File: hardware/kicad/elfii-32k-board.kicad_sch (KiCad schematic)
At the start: 14 parts, among them J1 ELFII_P3_86, SW1 RAM_PAGE_ENABLE, U1 74HC573, U2 CY62256-70PC, U3 74LS151, U4 CD4011

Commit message: Rewire Hyperboard-derived schematic from actual pin geometry
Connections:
- net ~MWR is gone; now on net MA0: J1.64 (MA0)
- net +5V: now also J1.1 (+5V), J1.2 (+5V), U1.20 (VCC), U2.28 (VCC), U3.16 (VCC), U4.14 (VDD); no longer J1.85 (DISP_STAT), J1.86 (BUS_CLK), SW1.1 (L0), SW1.2 (L1), SW1.3 (L2), SW1.4 (L3), SW1.5 (L4), SW1.6 (L5), SW1.7 (L6), SW1.8 (L7), U2.3 (A7)
- net A10: now also U1.14 (Q5), U2.21 (A10); no longer U1.16 (Q3), U2.2 (A12)
- net A12: now also U1.16 (Q3), U2.2 (A12), U3.11 (S0); no longer U1.14 (Q5), U2.21 (A10)
- net A13: now also U1.17 (Q2), U2.26 (A13), U3.10 (S1); no longer U1.13 (Q6), U2.24 (A9)
- net A14: now also U1.18 (Q1), U2.1 (A14), U3.9 (S2); no longer U1.12 (Q7), U2.25 (A8)
- net A15: now also JP1.1 (LOW=A15), U1.19 (Q0), U4.12 (4A), U4.13 (4B); no longer JP1.3 (HIGH=/A15), U4.8 (3A)
- net A15_N: now also JP1.3 (HIGH=/A15), U4.11 (4Y); no longer JP1.1 (LOW=A15)
- net A8: now also U1.12 (Q7), U2.25 (A8); no longer U1.18 (Q1), U2.1 (A14)
- net A9: now also U1.13 (Q6), U2.24 (A9); no longer U1.17 (Q2), U2.26 (A13)
- net D0: now also J1.62 (D0), U2.11 (D0); no longer J1.26 (SC0)
- net D1: now also J1.58 (D1), U2.12 (D1); no longer J1.30 (~MRD)
- net D2: now also J1.54 (D2), U2.13 (D2); no longer J1.34 (D7)
- net D3: now also J1.50 (D3), U2.15 (D3); no longer J1.38 (D6)
- net D4: now also J1.46 (D4), U2.16 (D4); no longer J1.42 (D5)
- net D5: now also J1.42 (D5), U2.17 (D5); no longer J1.46 (D4)
- net D6: now also J1.38 (D6), U2.18 (D6); no longer J1.50 (D3)
- net D7: now also J1.34 (D7), U2.19 (D7); no longer J1.54 (D2)
- net GND: now also J1.5 (GND), J1.80 (GND), RN1.1 (COM), U1.1 (~{OE}), U1.10 (GND), U2.14 (GND), U3.8 (GND), U4.1 (1A), U4.5 (2A), U4.6 (2B), U4.7 (VSS), U4.8 (3A), U4.9 (3B); no longer J1.8 (~CLOCK), J1.81 (SYNC), U2.4 (A6), U4.12 (4A)
- net HALF_EN: now also U3.7 (~{E})
- net MA0: now also U1.9 (D7), U2.10 (A0); no longer J1.24 (~MWR), U1.3 (D1)
- net MA1: now also J1.60 (MA1), U1.8 (D6), U2.9 (A1); no longer J1.28 (TPA), U1.4 (D2)
- net MA2: now also J1.56 (MA2), U1.7 (D5), U2.8 (A2); no longer J1.32 (TPB), U1.5 (D3)
- net MA3: now also J1.52 (MA3), U2.7 (A3); no longer J1.36 (MA7)
- net MA4: now also J1.48 (MA4), U1.5 (D3), U2.6 (A4); no longer J1.40 (MA6), U1.7 (D5)
- net MA5: now also U1.4 (D2), U2.5 (A5); no longer U1.8 (D6)
- net MA6: now also J1.40 (MA6), U1.3 (D1), U2.4 (A6); no longer J1.48 (MA4), U1.9 (D7), U2.14 (GND)
- net MA7: now also J1.36 (MA7), U1.2 (D0), U2.3 (A7); no longer J1.52 (MA3), U2.28 (VCC)
- net MB_RAM_DISABLE: now also J1.69 (MEMORY_OFF?); no longer J1.17 (X17)
- net PAGE0: now also RN1.2 (R0), SW1.16 (R0), U3.4 (I0); no longer RN1.9 (R7), SW1.9 (R7), U3.12 (I7)
- net PAGE1: now also RN1.3 (R1), SW1.15 (R1), U3.3 (I1); no longer RN1.8 (R6), SW1.10 (R6), U3.13 (I6)
- net PAGE2: now also RN1.4 (R2), SW1.14 (R2), U3.2 (I2); no longer RN1.7 (R5), SW1.11 (R5), U3.14 (I5)
- net PAGE3: now also RN1.5 (R3), SW1.13 (R3), U3.1 (I3); no longer RN1.6 (R4), SW1.12 (R4), U3.15 (I4)
- net PAGE4: now also RN1.6 (R4), SW1.12 (R4), U3.15 (I4); no longer RN1.5 (R3), SW1.13 (R3), U3.1 (I3)
- net PAGE5: now also RN1.7 (R5), SW1.11 (R5), U3.14 (I5); no longer RN1.4 (R2), SW1.14 (R2), U3.2 (I2)
- net PAGE6: now also RN1.8 (R6), SW1.10 (R6), U3.13 (I6); no longer RN1.3 (R1), SW1.15 (R1), U3.3 (I1)
- net PAGE7: now also RN1.9 (R7), SW1.9 (R7), U3.12 (I7); no longer RN1.2 (R0), SW1.16 (R0), U3.4 (I0)
- net RAM_CS_N: now also U2.20 (~{CS}), U3.6 (~{Z}); no longer U2.22 (~{OE}), U3.5 (Z)
- net TPA: now also J1.24 (~MWR), J1.28 (TPA), U1.11 (LE), U2.27 (~{WE}); no longer J1.58 (D1), J1.60 (MA1), U2.20 (~{CS})
- new net: SW1.1 (L0), SW1.2 (L1), SW1.3 (L2), SW1.4 (L3), SW1.5 (L4), SW1.6 (L5), SW1.7 (L6), SW1.8 (L7)
- new net ~MRD: J1.30 (~MRD), U2.22 (~{OE})
- no-connect marks 4 -> 66
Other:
- note added: "4K page enable / RAM chip select"
- note added: "74HC573 high-address latch (Hyperboard A8)"
- note added: "74LS151 + SW1 select 4K pages; JP1 selects LOW/HIGH 32K half"
- note added: "C1-C4 100n; C5 10u"
- note added: "CY62256 SRAM (Hyperboard A11)"
- note added: "Decoupling / local bulk"
- note added: "ELF II 86-contact expansion edge"
- note added: "ELF II edge -> TPA address latch -> CY62256; /MRD and /MWR are direct"
- note added: "JP1 1-2 = LOW 32K; 2-3 = HIGH 32K"
- note added: "JP2 DEFAULT OPEN"
- note added: "JP2 optionally grounds P3-69; leave OPEN until early-Netronics motherboard behavior is bench verified"
- note added: "RAM half select"
- note removed: "1802 bus -> TPA high-address latch -> CY62256; direct /MRD and /MWR"
- note removed: "C1-C4: one 100n bypass per IC; C5: local bulk"
- note removed: "JP1: 1-2 LOW 32K; 2-3 HIGH 32K"
- note removed: "JP2 default OPEN"
- note removed: "JP2 grounds P3-69 only when fitted; early Netronics behavior remains bench-unverified"
- note removed: "SW1 0000..7000 page enables"
- note removed: "SW1/U3 select 4K pages; JP1 selects LOW or HIGH 32K half"
- note removed: "U3 /Z -> SRAM /CS"
- note removed: "U4 gate 4: A15 NAND A15 = /A15"

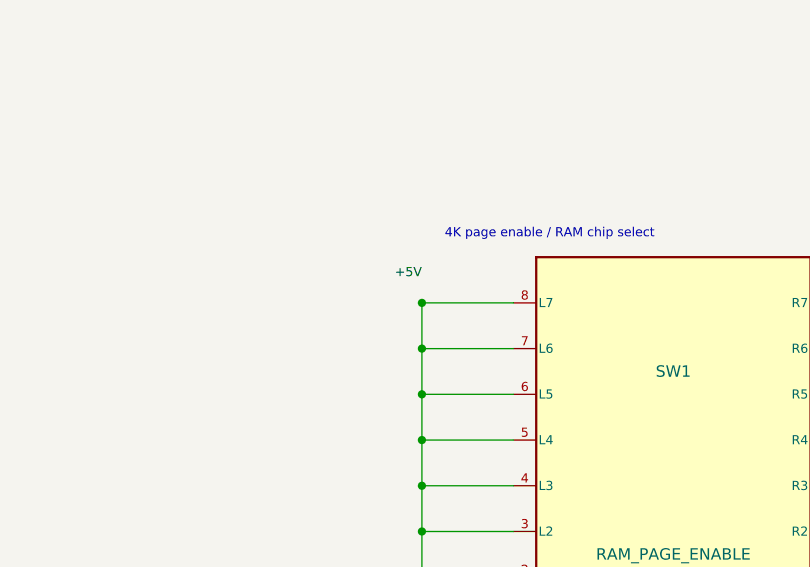
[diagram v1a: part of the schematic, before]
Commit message: Place page-switch supply label on its rail
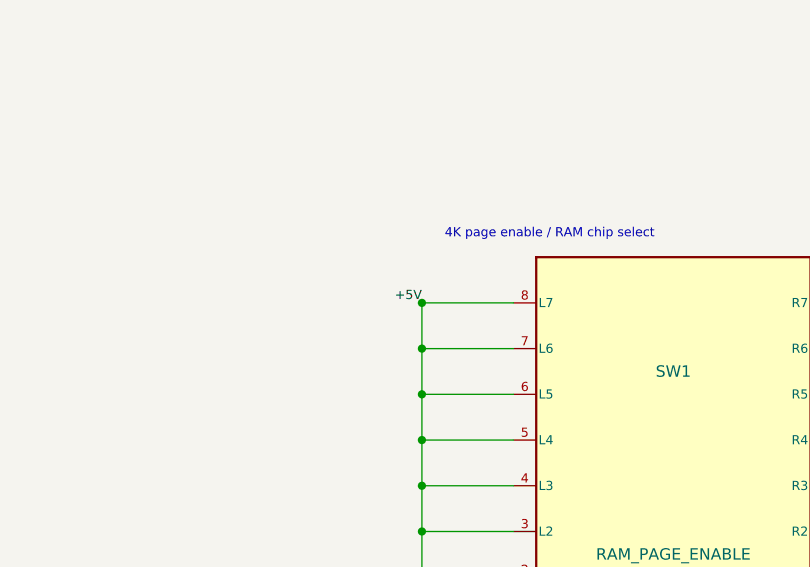
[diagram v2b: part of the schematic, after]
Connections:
- net +5V: now also SW1.1 (L0), SW1.2 (L1), SW1.3 (L2), SW1.4 (L3), SW1.5 (L4), SW1.6 (L5), SW1.7 (L6), SW1.8 (L7)
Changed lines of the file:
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@@
 (label "PAGE7" (at 226.06 236.22 0) (effects (font (size 1.016 1.016)) (justify left bottom)))
 (wire (pts (xy 175.26 236.22) (xy 175.26 271.78)) (stroke (width 0) (type default)))
-(label "+5V" (at 175.26 233.68 0) (effects (font (size 1.016 1.016)) (justify right bottom)))
+(label "+5V" (at 175.26 236.22 0) (effects (font (size 1.016 1.016)) (justify right bottom)))
 (wire (pts (xy 175.26 271.78) (xy 185.42 271.78)) (stroke (width 0) (type default)))
 (junction (at 175.26 271.78) (diameter 0) (color 0 0 0 0))
